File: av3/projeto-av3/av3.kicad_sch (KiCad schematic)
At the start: 0 parts

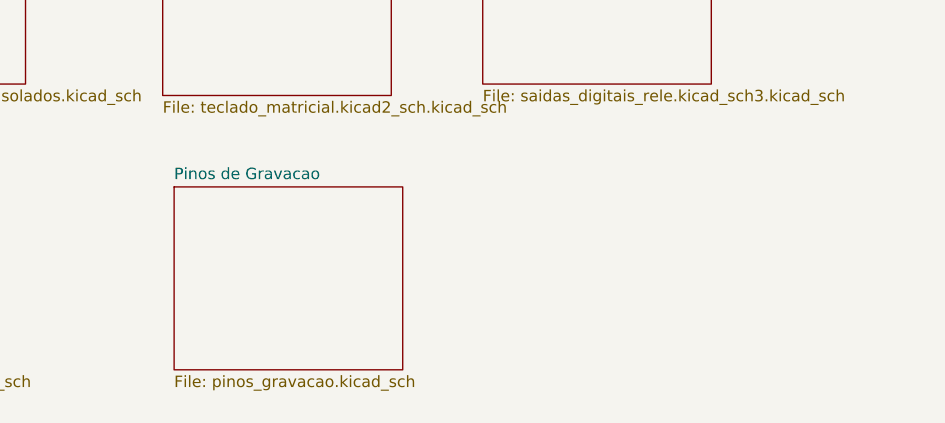
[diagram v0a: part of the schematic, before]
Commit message: Ligação do cristal no atmega2560 e início do esquemático das saídas digitais com relé.
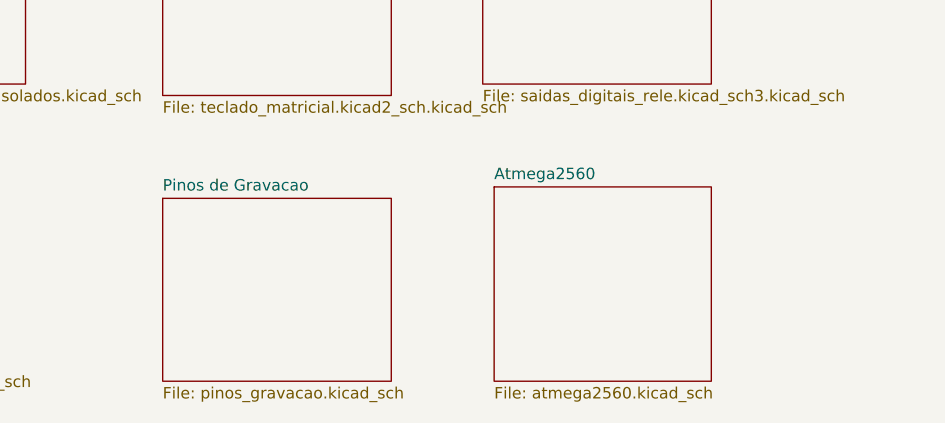
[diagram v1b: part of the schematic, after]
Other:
- added sheet Atmega2560 (atmega2560.kicad_sch)
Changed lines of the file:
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@@
+	)
+	(sheet
+		(at 105.41 60.96)
+		(size 24.13 21.59)
+		(fields_autoplaced yes)
+		(stroke
+			(width 0.1524)
+			(type solid)
+		)
+		(fill
+			(color 0 0 0 0.0000)
+		)
+		(property "Sheetname" "Atmega2560"
+			(at 105.41 60.2484 0)
+			(effects
+				(font
+					(size 1.27 1.27)
+				)
+				(justify left bottom)
+			)
+		)
+		(property "Sheetfile" "atmega2560.kicad_sch"
+			(at 105.41 83.1346 0)
+			(effects
+				(font
+					(size 1.27 1.27)
+				)
+				(justify left top)
+			)
+		)
+		(instances
+			(project "av3"
+				(path "/82998b71-606c-4e03-99b7-477e2a65cb94"
+					(page "7")
+				)
+			)
+		)
 	)
 	(sheet
@@
 	)
 	(sheet
-		(at 69.85 60.96)
+		(at 68.58 62.23)
 		(size 25.4 20.32)
 		(fields_autoplaced yes)
@@
 		)
 		(property "Sheetname" "Pinos de Gravacao"
-			(at 69.85 60.2484 0)
+			(at 68.58 61.5184 0)
 			(effects
 				(font
@@
 		)
 		(property "Sheetfile" "pinos_gravacao.kicad_sch"
-			(at 69.85 81.8646 0)
+			(at 68.58 83.1346 0)
 			(effects
 				(font

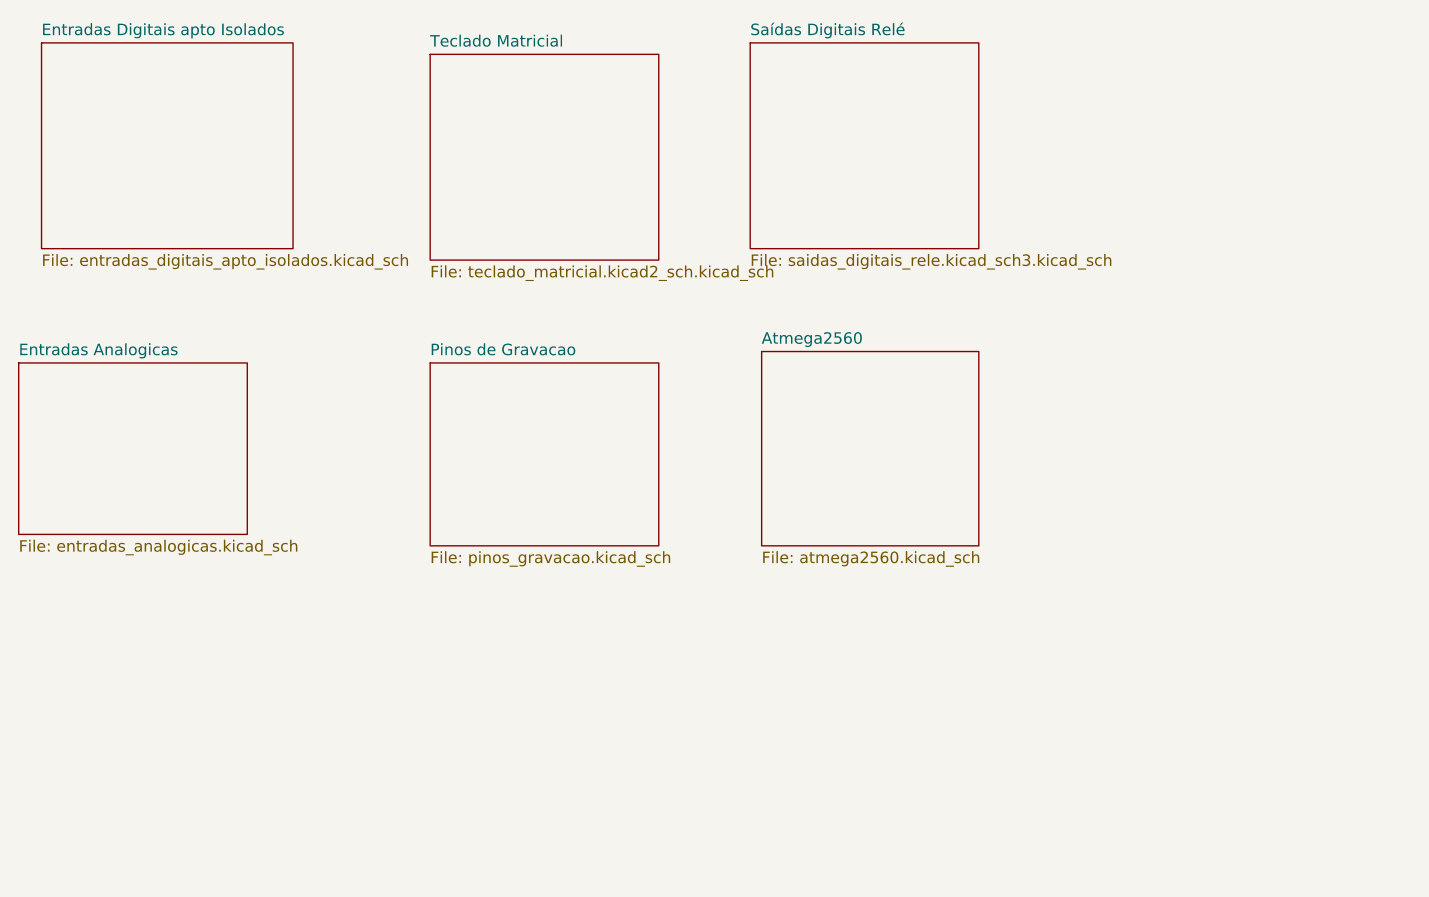
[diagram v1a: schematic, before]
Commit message: Maioria dos esquemáticos finalizados.
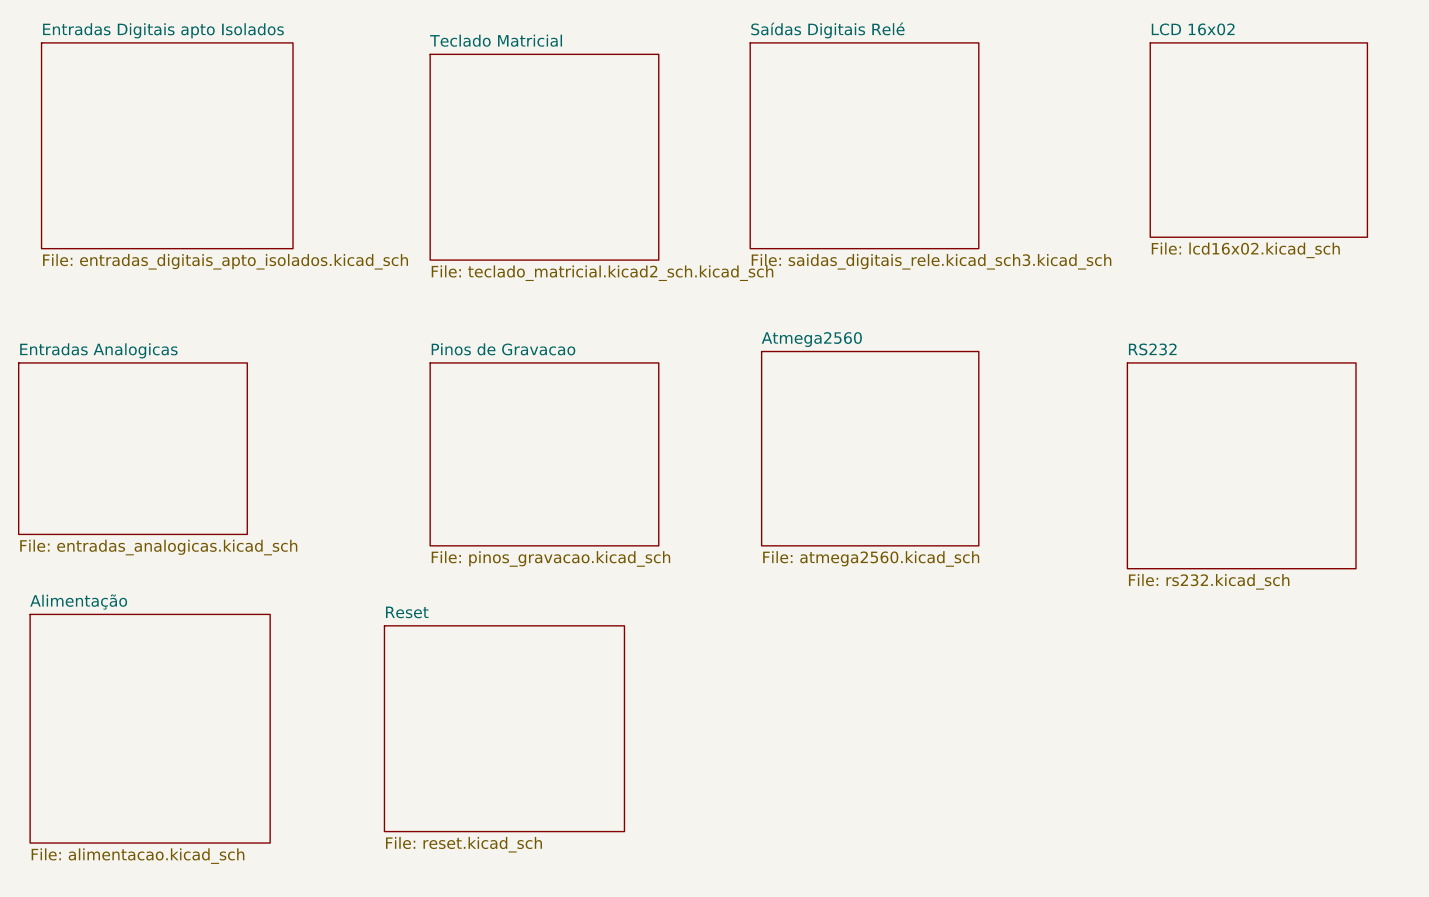
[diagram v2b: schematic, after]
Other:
- added sheet Alimentação (alimentacao.kicad_sch)
- added sheet LCD 16x02 (lcd16x02.kicad_sch)
- added sheet RS232 (rs232.kicad_sch)
- added sheet Reset (reset.kicad_sch)
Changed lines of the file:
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@@
+	)
+	(sheet
+		(at 148.59 26.67)
+		(size 24.13 21.59)
+		(fields_autoplaced yes)
+		(stroke
+			(width 0.1524)
+			(type solid)
+		)
+		(fill
+			(color 0 0 0 0.0000)
+		)
+		(property "Sheetname" "LCD 16x02"
+			(at 148.59 25.9584 0)
+			(effects
+				(font
+					(size 1.27 1.27)
+				)
+				(justify left bottom)
+			)
+		)
+		(property "Sheetfile" "lcd16x02.kicad_sch"
+			(at 148.59 48.8446 0)
+			(effects
+				(font
+					(size 1.27 1.27)
+				)
+				(justify left top)
+			)
+		)
+		(instances
+			(project "av3"
+				(path "/82998b71-606c-4e03-99b7-477e2a65cb94"
+					(page "8")
+				)
+			)
+		)
+	)
+	(sheet
+		(at 24.13 90.17)
+		(size 26.67 25.4)
+		(fields_autoplaced yes)
+		(stroke
+			(width 0.1524)
+			(type solid)
+		)
+		(fill
+			(color 0 0 0 0.0000)
+		)
+		(property "Sheetname" "Alimentação"
+			(at 24.13 89.4584 0)
+			(effects
+				(font
+					(size 1.27 1.27)
+				)
+				(justify left bottom)
+			)
+		)
+		(property "Sheetfile" "alimentacao.kicad_sch"
+			(at 24.13 116.1546 0)
+			(effects
+				(font
+					(size 1.27 1.27)
+				)
+				(justify left top)
+			)
+		)
+		(instances
+			(project "av3"
+				(path "/82998b71-606c-4e03-99b7-477e2a65cb94"
+					(page "10")
+				)
+			)
+		)
 	)
 	(sheet
@@
 	)
 	(sheet
+		(at 146.05 62.23)
+		(size 25.4 22.86)
+		(fields_autoplaced yes)
+		(stroke
+			(width 0.1524)
+			(type solid)
+		)
+		(fill
+			(color 0 0 0 0.0000)
+		)
+		(property "Sheetname" "RS232"
+			(at 146.05 61.5184 0)
+			(effects
+				(font
+					(size 1.27 1.27)
+				)
+				(justify left bottom)
+			)
+		)
+		(property "Sheetfile" "rs232.kicad_sch"
+			(at 146.05 85.6746 0)
+			(effects
+				(font
+					(size 1.27 1.27)
+				)
+				(justify left top)
+			)
+		)
+		(instances
+			(project "av3"
+				(path "/82998b71-606c-4e03-99b7-477e2a65cb94"
+					(page "9")
+				)
+			)
+		)
+	)
+	(sheet
 		(at 105.41 60.96)
 		(size 24.13 21.59)
@@
 				)
 			)
+		)
+	)
+	(sheet
+		(at 63.5 91.44)
+		(size 26.67 22.86)
+		(fields_autoplaced yes)
+		(stroke
+			(width 0.1524)
+			(type solid)
+		)
+		(fill
+			(color 0 0 0 0.0000)
+		)
+		(property "Sheetname" "Reset"
+			(at 63.5 90.7284 0)
+			(effects
+				(font
+					(size 1.27 1.27)
+				)
+				(justify left bottom)
+			)
+		)
+		(property "Sheetfile" "reset.kicad_sch"
+			(at 63.5 114.8846 0)
+			(effects
+				(font
+					(size 1.27 1.27)
+				)
+				(justify left top)
+			)
+		)
+		(instances
+			(project "av3"
+				(path "/82998b71-606c-4e03-99b7-477e2a65cb94"
+					(page "11")
+				)
+			)

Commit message: Esquemático finalizado, faltando somente o PCB.
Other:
- added sheet Crystal (crystal.kicad_sch)
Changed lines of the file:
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@@
+	)
+	(sheet
+		(at 102.87 93.98)
+		(size 26.67 22.86)
+		(fields_autoplaced yes)
+		(stroke
+			(width 0.1524)
+			(type solid)
+		)
+		(fill
+			(color 0 0 0 0.0000)
+		)
+		(property "Sheetname" "Crystal"
+			(at 102.87 93.2684 0)
+			(effects
+				(font
+					(size 1.27 1.27)
+				)
+				(justify left bottom)
+			)
+		)
+		(property "Sheetfile" "crystal.kicad_sch"
+			(at 102.87 117.4246 0)
+			(effects
+				(font
+					(size 1.27 1.27)
+				)
+				(justify left top)
+			)
+		)
+		(instances
+			(project "av3"
+				(path "/82998b71-606c-4e03-99b7-477e2a65cb94"
+					(page "12")
+				)
+			)
+		)
 	)
 	(sheet
